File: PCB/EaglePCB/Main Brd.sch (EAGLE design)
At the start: 70 parts, among them J2 702461401, U1 ATWINC1500-MR210PB1952-T, U3 MSP430FR2355TDBTRDBT0038A_M, U6 ARJM11C7-114-BA-EW2

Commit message: pcb moving forward
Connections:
- net LORA1_TX renamed LORA1_RX
- net LORA2_RX renamed LORA2_TX
- removed net A1_CLK: U3.P4.1_UCA1CLK
- removed net A1_MISO: U3.P4.2_UCA1RXD_UCA1SOMI_UCA1RXD_N
- removed net A1_MOSI: U3.P4.3_UCA1TXD_UCA1SIMO_UCA1TXD_N
- removed net ATC_SSN: U1.SPI_SSN
- removed net B0_CLK: U3.P1.1_UCB0CLK_ACLK_OA0O_COMP0.1_A1
- removed net B0_MISO: U3.P1.2_UCB0SIMO_UCB0SDA_TB0TRG_OA0-_A2_VEREF-
- removed net B0_MOSI: U3.P1.3_UCB0SOMI_OA0+_A3
- removed net B1_CLK: U3.P4.5_UCB1CLK
- removed net B1_MISO: U3.P4.6_UCB1SIMO_UCB1SDA
- removed net B1_MOSI: U3.P4.7_UCB1SOMI_UCB1SCL
- removed net MSP_TCK: J2.7, U3.P1.4_UCA0STE_TCK_A4
- removed net N$21: U3.P4.0_UCA1STE_ISOTXD_ISORXD
- removed net SPI_SCK: U1.SPI_SCK
- new net ATC_CHIPSEL: U1.SPI_SSN, U3.P4.0_UCA1STE_ISOTXD_ISORXD
- new net ATC_SCK: U1.SPI_SCK, U3.P4.1_UCA1CLK
- net !ATC_IRQ: now also U3.P3.4_SMCLK
- net !ATC_RST: now also U3.P3.2_OA2-
- net !ETH_CHIPSEL: now also J2.7, U3.P1.4_UCA0STE_TCK_A4
- net !ETH_IRQ: now also U3.P2.1_TB1.2_COMP1.O
- net !ETH_RST: now also U3.P2.0_TB1.1_COMP0.O
- net ATC_MISO: now also U3.P4.2_UCA1RXD_UCA1SOMI_UCA1RXD_N
- net ATC_MOSI: now also U3.P4.3_UCA1TXD_UCA1SIMO_UCA1TXD_N
- net LORA1_CHIPSEL: now also U3.P4.4_UCB1STE
- net LORA1_IRQ: now also U3.P3.1_OA2O
- net LORA1_MISO: now also U3.P4.7_UCB1SOMI_UCB1SCL
- net LORA1_MOSI: now also U3.P4.6_UCB1SIMO_UCB1SDA
- net LORA1_RST: now also U3.P3.0_MCLK
- net LORA1_SCK: now also U3.P4.5_UCB1CLK
- net LORA2_CHIPSEL: now also U3.P1.0_UCB0STE_SMCLK_COMP0.0_A0_VEREF+
- net LORA2_IRQ: now also U3.P2.4_COMP1.1
- net LORA2_MISO: now also U3.P1.3_UCB0SOMI_OA0+_A3
- net LORA2_MOSI: now also U3.P1.2_UCB0SIMO_UCB0SDA_TB0TRG_OA0-_A2_VEREF-
- net LORA2_RST: now also U3.P2.2_TB1CLK
- net LORA2_SCK: now also U3.P1.1_UCB0CLK_ACLK_OA0O_COMP0.1_A1
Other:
- note added: "Receive"
- note added: "Send"

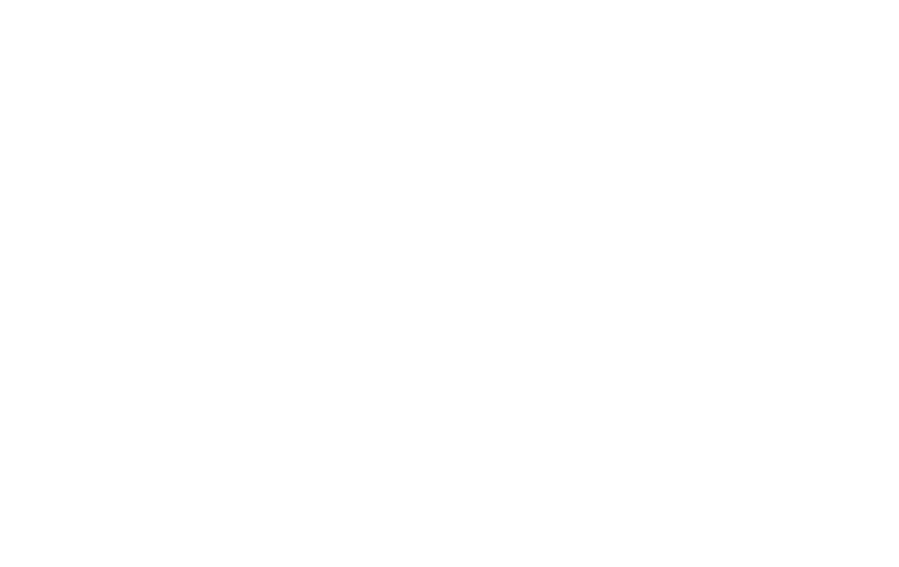
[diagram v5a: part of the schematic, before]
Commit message: added barrel connection
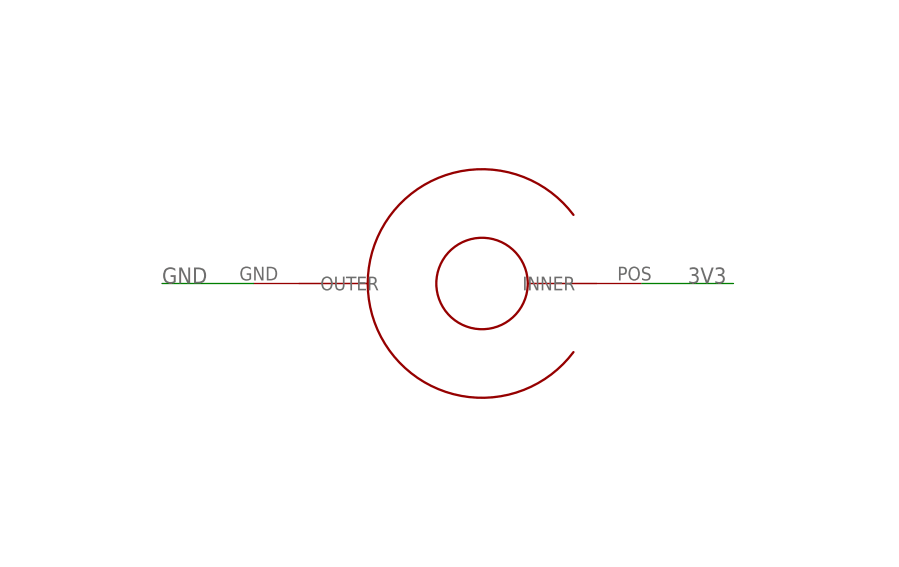
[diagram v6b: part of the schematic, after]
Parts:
- added U$7: BARREL_CONN_EXTERN, 473:BARREL_CONN_EXTERN
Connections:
- net 3V3: now also U$7.INNER
- net GND: now also U$7.OUTER
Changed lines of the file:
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@@
 <part name="X1" library="adafruit" library_urn="urn:adsk.eagle:library:420" deviceset="SMACONNECTOR" device="_EDGE" package3d_urn="urn:adsk.eagle:package:6240945/1"/>
 <part name="X2" library="adafruit" library_urn="urn:adsk.eagle:library:420" deviceset="SMACONNECTOR" device="_EDGE" package3d_urn="urn:adsk.eagle:package:6240945/1"/>
+<part name="U$7" library="473" deviceset="BARREL_CONN_EXTERN" device=""/>
 </parts>
 <sheets>
@@
 <attribute name="VALUE" x="-129.54" y="287.02" size="1.27" layer="95" rot="R180"/>
 </instance>
+<instance part="U$7" gate="G$1" x="101.6" y="91.44" smashed="yes"/>
 </instances>
 <busses>
@@
 <label x="248.92" y="63.5" size="1.778" layer="95" rot="R90"/>
 </segment>
+<segment>
+<pinref part="U$7" gate="G$1" pin="OUTER"/>
+<wire x1="76.2" y1="91.44" x2="66.04" y2="91.44" width="0.1524" layer="91"/>
+<label x="66.04" y="91.44" size="1.778" layer="95"/>
+</segment>
 </net>
 <net name="RFI" class="0">
@@
 <label x="213.36" y="-35.56" size="1.778" layer="95"/>
 </segment>
-</net>
+<segment>
+<pinref part="U$7" gate="G$1" pin="INNER"/>
+<wire x1="119.38" y1="91.44" x2="129.54" y2="91.44" width="0.1524" layer="91"/>
+<label x="124.46" y="91.44" size="1.778" layer="95"/>
+</segment>
+</net>
